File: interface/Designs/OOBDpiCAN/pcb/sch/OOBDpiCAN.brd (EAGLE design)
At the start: 65.1 x 57.3 mm, 143 parts, among them IC1 ADM3053M, IC5 DS3231, IC6 EEPROM24, IC7 ADM3053M, Q1 12MHz, Q2 16MHz

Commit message: first roughly placing of ADM3053
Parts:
- removed $$U$13, U$11, U$9: MCP2551SO8, can:SO08
- removed BAT2: (no value), SparkFun:BATTCON_12MM_PTH
- removed C61: 10u, rcl:C0805K
- removed C62: 100n, rcl:C0805K
- removed U$10, U$12, U$7: (no value), SparkFun-Connectors:SCREWTERMINAL-3.5MM-3
- removed U$6: STM32F042CT, micro-stm_v3:LQFP48
- removed U$8: (no value), jumper:JP5
- added BAT1: (no value), SparkFun:BATTCON_12MM_PTH
- added C47: NA(47nF), resistor:C0603
- added C48: NA(10nF), resistor:C0603
- added C49: 33pF, resistor:C0603
- added C52: 100nF, resistor:C0603
- added IC10, IC3, IC4, IC9: MCP2551SO8, can:SO08
- added IC11: EEPROM24, FLYFISH:SOIC8
- added IC12: DS3231, DS3231_industrialberry:SOIC-16W
- added IC2, IC8: STM32F042CT, micro-stm_v3:LQFP48
- C1, C2: value 33pF -> 100nF
- C11, C12: value 100nF -> 18pF
- C13, C14, C19, C20: value 100nF -> 100n; device resistor:C0603 -> rcl:C0603K
- C15, C16, C27, C29: value 100nF -> 10u; device resistor:C0603 -> rcl:C0805K
- C17, C18: value 100nF -> 10n; device resistor:C0603 -> rcl:C0603K
- C23, C24: value 100nF -> NA (AY2221K29Y5SS63L7); device resistor:C0603 -> rcl:C075-032X103
- C25, C26: value 100nF -> 100n; device resistor:C0603 -> rcl:C0805K
- C28: value 22uF/6.3V -> NA(10nF); device rcl:SMC_A -> resistor:C0603
- C30: value 18pF -> NA(10nF)
- C31: value 18pF -> 10n; device resistor:C0603 -> rcl:C0805K
- C32: value 100nF -> 10n; device resistor:C0603 -> rcl:C0805K
- C33: value 1uF -> 100n; device resistor:C0603 -> rcl:C0805K
- C34: value 10n -> 100n; device rcl:C0603K -> rcl:C0805K
- C35, C38: value 100n -> 100nF; device rcl:C0603K -> resistor:C0603
- C36, C43, C57: value 10u -> 100nF; device rcl:C0805K -> resistor:C0603
- C37, C41: value NA(10nF) -> 100nF
- C39, C44, C59: value 100n -> 100nF; device rcl:C0805K -> resistor:C0603
- C42: value 10n -> 100nF; device rcl:C0805K -> resistor:C0603
- C46: value NA(47nF) -> 100nF
- C50: device resistor:C0603 -> rcl:C0603
- C51: value NA(10nF) -> 33pF
- C53: value 1uF -> 100nF; device rcl:C0603 -> resistor:C0603
- C54: device rcl:C0603 -> resistor:C0603
- C55: value 10n -> 1uF; device rcl:C0603K -> resistor:C0603
- C56: value 100n -> 1uF; device rcl:C0603K -> rcl:C0603
- C58: value 100n -> 22uF/6.3V; device rcl:C0603K -> rcl:SMC_A
- C60: value 10n -> 22uF/6.3V; device rcl:C0805K -> rcl:SMC_A
- C9: value 22uF/6.3V -> 100nF; device rcl:SMC_A -> resistor:C0603
- IC1, IC7: value ADM3053M -> STM32F042CT; device ADM3053:SO20W -> micro-stm_v3:LQFP48
- IC5: value DS3231 -> ADM3053M; device DS3231_industrialberry:SOIC-16W -> ADM3053:SO20W
- IC6: value EEPROM24 -> ADM3053M; device FLYFISH:SOIC8 -> ADM3053:SO20W
- LED2, LED4: value yellow -> green
- LED5, LED7: value green -> yellow
- Q1: value 12MHz -> 16MHz
- Q2: value 16MHz -> 12MHz
- R1, R2: value 10k -> 510R
- R10: value 510R -> 0R; device resistor:R0603 -> rcl:0207/10
- R11: value 510R -> 8.2k; device resistor:R0603 -> rcl:R0603
- R12: value 120R -> 8.2k; device resistor:R0603 -> rcl:R0603
- R13, R14, R15: value 120R -> 60R
- R16: value 10k -> 60R
- R17: value NA(47k) -> 510R
- R18: value 680R -> 510R
- R19: value 10k -> 120R
- R20, R21, R22: value 60R -> 120R
- R27: value 10k -> 680R; device rcl:R0603 -> resistor:R0603
- R3, R4: value 510R -> 120R
- R31: value 8.2k -> 10k; device rcl:R0603 -> resistor:R0603
- R32: value 8.2k -> NA(47k); device rcl:R0603 -> resistor:R0603
- R33, R34, R36: value 0R -> 10k; device rcl:0207/10 -> resistor:R0603
- R35: value 0R -> 10k; device rcl:0207/10 -> rcl:R0603
- R7, R8: value 120R -> 0R; device resistor:R0603 -> rcl:0207/10
- R9: value 60R -> 0R; device resistor:R0603 -> rcl:0207/10
- U$1: value MCP2551SO8 -> (none); device can:SO08 -> jumper:JP5
- U$2, U$4: value STM32F042CT -> (none); device micro-stm_v3:LQFP48 -> SparkFun-Connectors:SCREWTERMINAL-3.5MM-3
- U$3: value GL850G-31 -> (none); device pimoroni:TSSOP28 -> SparkFun-Connectors:SCREWTERMINAL-3.5MM-3
- U$5: value STM32F042CT -> GL850G-31; device micro-stm_v3:LQFP48 -> pimoroni:TSSOP28
- moved C23 136.9 mm to (41.3, 17.8), turned to 90 degrees
- moved C41 125.9 mm to (-105.4, 45.7)
- moved C24 125.1 mm to (22.9, 17.8), turned to 90 degrees
- moved C57 121.8 mm to (-95.2, 39.4), turned to 0 degrees
- moved C54 119.9 mm to (-88.9, 39.4)
- moved R36 117.7 mm to (-88.9, 33.0), turned to 0 degrees
- moved C37 115.3 mm to (-80.0, 45.7)
- moved R16 112.3 mm to (25.4, 6.99)
- moved JP7 110.9 mm to (57.1, 7.62), turned to 90 degrees
- moved JP8 110.9 mm to (50.8, 7.62), turned to 90 degrees
- moved R23 100.5 mm to (-8.89, 39.4)
- moved R24 100.5 mm to (-109.2, 33.0)
- moved C38 98.4 mm to (-86.4, 45.7)
- moved C28 97.3 mm to (14.6, 7.62)
- moved R15 95.6 mm to (25.4, 9.53)
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- renumbered $$U$14 to $$U$1, SJ2 to SJ1
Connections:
- net +3V3: now also C1.1, C18.1, C2.1, C3.1, C36.1, C37.1, C38.1, C39.1, C4.1, C40.1, C41.1, C42.1, C43.1, C44.1, C5.1, C56.2, C6.1, C9.1, IC1.1, IC1.24, IC1.36, IC1.48, IC1.9, IC12.2, IC2.1, IC2.24, IC2.36, IC2.48, IC2.9, IC5.6, IC6.6, IC7.1, IC7.24, IC7.36, IC7.48, IC7.9, IC8.1, IC8.24, IC8.36, IC8.48, IC8.9, JP6.1, R35.2, U$1.1; no longer C11.1, C12.1, C13.1, C14.1, C15.1, C16.1, C21.1, C22.1, C23.1, C24.1, C25.1, C26.1, C27.1, C29.1, C34.1, C53.2, C55.1, C56.1, IC1.6, IC5.2, IC7.6, JP4.1, R27.2, U$2.1, U$2.24, U$2.36, U$2.48, U$2.9, U$4.1, U$4.24, U$4.36, U$4.48, U$4.9, U$5.1, U$5.24, U$5.36, U$5.48, U$5.9, U$6.1, U$6.24, U$6.36, U$6.48, U$6.9, U$8.1
- net +5V: now also C13.1, C14.1, C15.1, C16.1, C21.1, C22.1, C46.1, C50.2, C59.1, C60.+, IC10.3, IC11.8, IC3.3, IC4.3, IC5.8, IC9.3, R31.1, U$5.23; no longer $$U$13.3, C18.1, C28.+, C32.1, C36.1, C38.1, C40.1, C50.1, C54.2, C57.1, C58.1, IC1.8, IC7.8, R16.1, U$1.3, U$11.3, U$3.23, U$9.3
- net BOOT0: now also IC1.44, IC2.44, IC7.44, IC8.44, JP6.2, R1.2, R17.2, R18.2, R2.2; no longer JP4.2, R10.2, R11.2, R3.2, R4.2, U$2.44, U$4.44, U$5.44, U$6.44
- net CAN0-H: now also IC5.17, R14.1, R8.2, U$2.2; no longer IC7.17, R21.1, R34.2, U$10.2
- net CAN0-L: now also IC5.15, JP3.2, R7.2, U$2.1; no longer IC7.15, JP6.2, R33.2, U$10.1
- net CAN0_RXD: now also IC1.45, IC3.4, IC5.4; no longer IC7.4, U$2.45, U$9.4
- net CAN0_TXD: now also IC1.46, IC3.1, IC5.5; no longer IC7.5, U$2.46, U$9.1
- net CAN1-H: now also IC6.17, R10.2, R16.1, U$3.2; no longer IC1.17, R20.1, R36.2, U$7.2
- net CAN1-L: now also IC6.15, JP4.2, R9.2, U$3.1; no longer IC1.15, JP3.2, R35.2, U$7.1
- net CAN1_RXD: now also IC2.45, IC4.4, IC6.4; no longer IC1.4, U$1.4, U$4.45
- net CAN1_TXD: now also IC2.46, IC4.1, IC6.5; no longer IC1.5, U$1.1, U$4.46
- net CAN2-H: now also IC9.7, R24.1, U$4.2; no longer R23.1, U$11.7, U$12.2
- net CAN2-L: now also IC9.6, U$4.1; no longer U$11.6, U$12.1
- net CAN3-H: now also IC10.7, R26.1; no longer $$U$13.7, R25.1
- net CAN3-L: now also IC10.6; no longer $$U$13.6
- net GND: now also BAT1.GND, C23.1, C24.1, C28.2, C39.2, C42.2, C43.2, C44.2, C47.2, C48.2, C49.2, C50.1, C52.2, C53.2, C54.2, C56.1, C58.-, C59.2, C60.-, C9.2, IC1.23, IC1.35, IC1.47, IC1.8, IC10.2, IC10.8, IC11.1, IC11.2, IC11.3, IC11.4, IC12.10, IC12.11, IC12.12, IC12.13, IC12.5, IC12.6, IC12.7, IC12.8, IC12.9, IC2.23, IC2.35, IC2.47, IC2.8, IC3.2, IC3.8, IC4.2, IC4.8, IC5.1, IC5.3, IC6.10, IC6.7, IC6.9, IC7.23, IC7.35, IC7.47, IC7.8, IC8.23, IC8.35, IC8.47, IC8.8, IC9.2, IC9.8, R1.1, R2.1, R20.1, R21.1, R22.1, R27.1, R32.1, R36.1, U$1.3, U$2.3, U$3.3, U$4.3, U$5.14, U$5.15; no longer $$U$13.2, $$U$13.8, BAT2.GND, C23.2, C24.2, C25.2, C26.2, C27.2, C28.-, C29.2, C31.2, C32.2, C33.2, C34.2, C50.2, C53.1, C54.1, C56.2, C58.2, C9.-, IC1.1, IC1.10, IC1.3, IC1.7, IC1.9, IC5.11, IC5.12, IC5.13, IC5.5, IC5.6, IC5.8, IC6.2, IC6.4, IC7.1, IC7.10, IC7.3, IC7.7, IC7.9, R10.1, R11.1, R12.1, R13.1, R14.1, R15.1, R7.1, R8.1, U$1.2, U$1.8, U$10.3, U$11.2, U$11.8, U$12.3, U$2.23, U$2.35, U$2.47, U$2.8, U$3.14, U$3.15, U$4.23, U$4.35, U$4.47, U$4.8, U$5.23, U$5.35, U$5.47, U$5.8, U$6.23, U$6.35, U$6.47, U$6.8, U$7.3, U$8.3, U$9.2, U$9.8
- net GNDA: now also C23.2, C24.2, C25.2, C26.2, C27.2, C29.2, C31.2, C32.2, C33.2, C34.2, IC5.11, IC5.13, IC5.16, IC5.20, IC6.11, IC6.13, IC6.16, IC6.20, R11.1, R12.1; no longer C39.2, C42.2, C43.2, C44.2, C59.2, C60.2, C61.2, C62.2, IC1.11, IC1.13, IC1.16, IC1.20, IC7.11, IC7.13, IC7.16, IC7.20, R31.1, R32.1
- net ID_SC: now also IC11.6, R29.2; no longer IC6.6, R28.2
- net ID_SD: now also IC11.5, R30.2; no longer IC6.5, R29.2
- net INT-: now also IC12.3, R35.1; no longer IC5.3, R27.1
- net MC0_1: now also IC2.29, IC7.5; no longer U$4.29, U$5.5
- net MCO_0: now also IC1.29; no longer U$2.29
- net MCO_1: now also IC2.5; no longer U$4.5
- net MCO_2: now also IC7.29, IC8.5; no longer U$5.29, U$6.5
- net N$1: now also IC5.18, R11.2; no longer IC7.18, R31.2
- net N$10: now also C12.1, IC1.6, Q1.2; no longer C31.1, Q2.2, U$2.6
- net N$11: now also C11.1, IC1.5, Q1.1; no longer C30.1, Q2.1, U$2.5
- net N$12: now also IC6.18, R12.2; no longer IC1.18, R32.2
- net N$13: now also C26.1, C29.1, C32.1, C34.1, IC6.12, IC6.19; no longer C39.1, C42.1, C43.1, C44.1, IC1.12, IC1.19
- net N$14: now also IC3.6, R7.1; no longer R33.1, U$9.6
- net N$15: now also IC8.19, LED7.A; no longer LED4.A, U$6.19
- net N$16: now also IC8.18; no longer U$6.18
- net N$17: now also LED7.C, R21.2; no longer LED4.C, R14.2
- net N$18: now also R22.2; no longer R15.2
- net N$19: now also IC3.7, R8.1; no longer R34.1, U$9.7
- net N$2: now also C51.1, Q2.2, U$5.7; no longer C1.1, Q1.2, U$3.7
- net N$20: now also C47.1; no longer C46.1
- net N$21: now also IC10.4, IC8.45; no longer $$U$13.4, U$6.45
- net N$22: now also IC1.19; no longer U$2.19
- net N$23: now also IC1.18, LED2.A; no longer LED5.A, U$2.18
- net N$24: now also R3.2; no longer R5.2
- net N$25: now also LED2.C, R4.2; no longer LED5.C, R6.2
- net N$26: now also IC4.7, R10.1; no longer R36.1, U$1.7
- net N$27: now also IC4.6, R9.1; no longer R35.1, U$1.6
- net N$28: now also JP4.1, R15.1; no longer JP3.1, R9.1
- net N$29: now also IC2.19, LED3.A; no longer LED2.A, U$4.19
- net N$3: now also C49.1, Q2.1, U$5.6; no longer C2.1, Q1.1, U$3.6
- net N$30: now also IC2.18, LED4.A; no longer LED6.A, U$4.18
- net N$31: now also LED3.C, R5.2; no longer LED2.C, R7.2
- net N$32: now also LED4.C, R6.2; no longer LED6.C, R8.2
- net N$33: now also C57.1, C58.+, R33.2, R34.2, U$5.16, U$5.24; no longer C6.1, C9.+, R1.2, R2.2, U$3.16, U$3.24
- net N$34: now also R33.1, U$5.18; no longer R2.1, U$3.18
- net N$35: now also R34.1, U$5.17; no longer R1.1, U$3.17
- net N$36: now also C55.1, R31.2, R32.2, U$5.13; no longer C33.1, R16.2, R17.2, U$3.13
- net N$37: now also U$5.26; no longer U$3.26
- net N$38: now also U$5.25; no longer U$3.25
- net N$39: now also C52.1, C53.1, C54.1, U$5.1, U$5.10, U$5.5; no longer C3.1, C4.1, C5.1, U$3.1, U$3.10, U$3.5
- net N$4: now also IC7.19, LED5.A; no longer LED3.A, U$5.19
- net N$40: now also R27.2, U$5.4; no longer R18.2, U$3.4
- net N$44: now also R36.2; no longer R19.2
- net N$48: now also JP3.1, R13.1; no longer JP6.1, R22.1
- net N$49: now also C30.1, R15.2, R16.2; no longer C37.1, R20.2, R9.2
- net N$5: now also IC11.7, R28.2; no longer IC6.7, R30.2
- net N$53: now also C28.1, R13.2, R14.2; no longer C41.1, R21.2, R22.2
- net N$54: now also IC10.1, IC8.46; no longer $$U$13.1, U$6.46
- net N$56: now also IC7.45, IC9.4; no longer U$11.4, U$5.45
- net N$57: now also IC7.46, IC9.1; no longer U$11.1, U$5.46
- net N$59: now also R25.1; no longer R26.1
- net N$6: now also R23.1; no longer R24.1
- net N$63: now also C48.1; no longer C51.1
- net N$65: now also C25.1, C27.1, C31.1, C33.1, IC5.12, IC5.19; no longer C59.1, C60.1, C61.1, C62.1, IC7.12, IC7.19
- net N$7: now also IC7.18, LED6.A; no longer LED7.A, U$5.18
- net N$8: now also LED5.C, R19.2; no longer LED3.C, R12.2
- net N$9: now also LED6.C, R20.2; no longer LED7.C, R13.2
- net NRST: now also IC1.7, IC2.7, IC7.7, U$1.5; no longer U$2.7, U$4.7, U$5.7, U$8.5
- net NRST1: now also IC8.7; no longer U$6.7
- net SCL: now also IC12.16; no longer IC5.16
- net SDA: now also IC12.15; no longer IC5.15
- net SWCLK: now also IC1.37, IC2.37, IC7.37, U$1.2; no longer U$2.37, U$4.37, U$5.37, U$8.2
- net SWCLK1: now also IC8.37; no longer U$6.37
- net SWDIO: now also IC1.34, IC2.34, IC7.34, U$1.4; no longer U$2.34, U$4.34, U$5.34, U$8.4
- net SWDIO1: now also IC8.34; no longer U$6.34
- net USB0_DM: now also IC1.32, U$5.27; no longer U$2.32, U$3.27
- net USB0_DP: now also IC1.33, U$5.28; no longer U$2.33, U$3.28
- net USB1_DM: now also IC2.32, U$5.2; no longer U$3.2, U$4.32
- net USB1_DP: now also IC2.33, U$5.3; no longer U$3.3, U$4.33
- net USB2_DM: now also IC7.32, U$5.8; no longer U$3.8, U$5.32
- net USB2_DP: now also IC7.33, U$5.9; no longer U$3.9, U$5.33
- net USB3_DM: now also IC8.32, U$5.11; no longer U$3.11, U$6.32
- net USB3_DP: now also IC8.33, U$5.12; no longer U$3.12, U$6.33
- net VBAT: now also BAT1.VCC@1, IC12.14; no longer BAT2.VCC@1, IC5.14

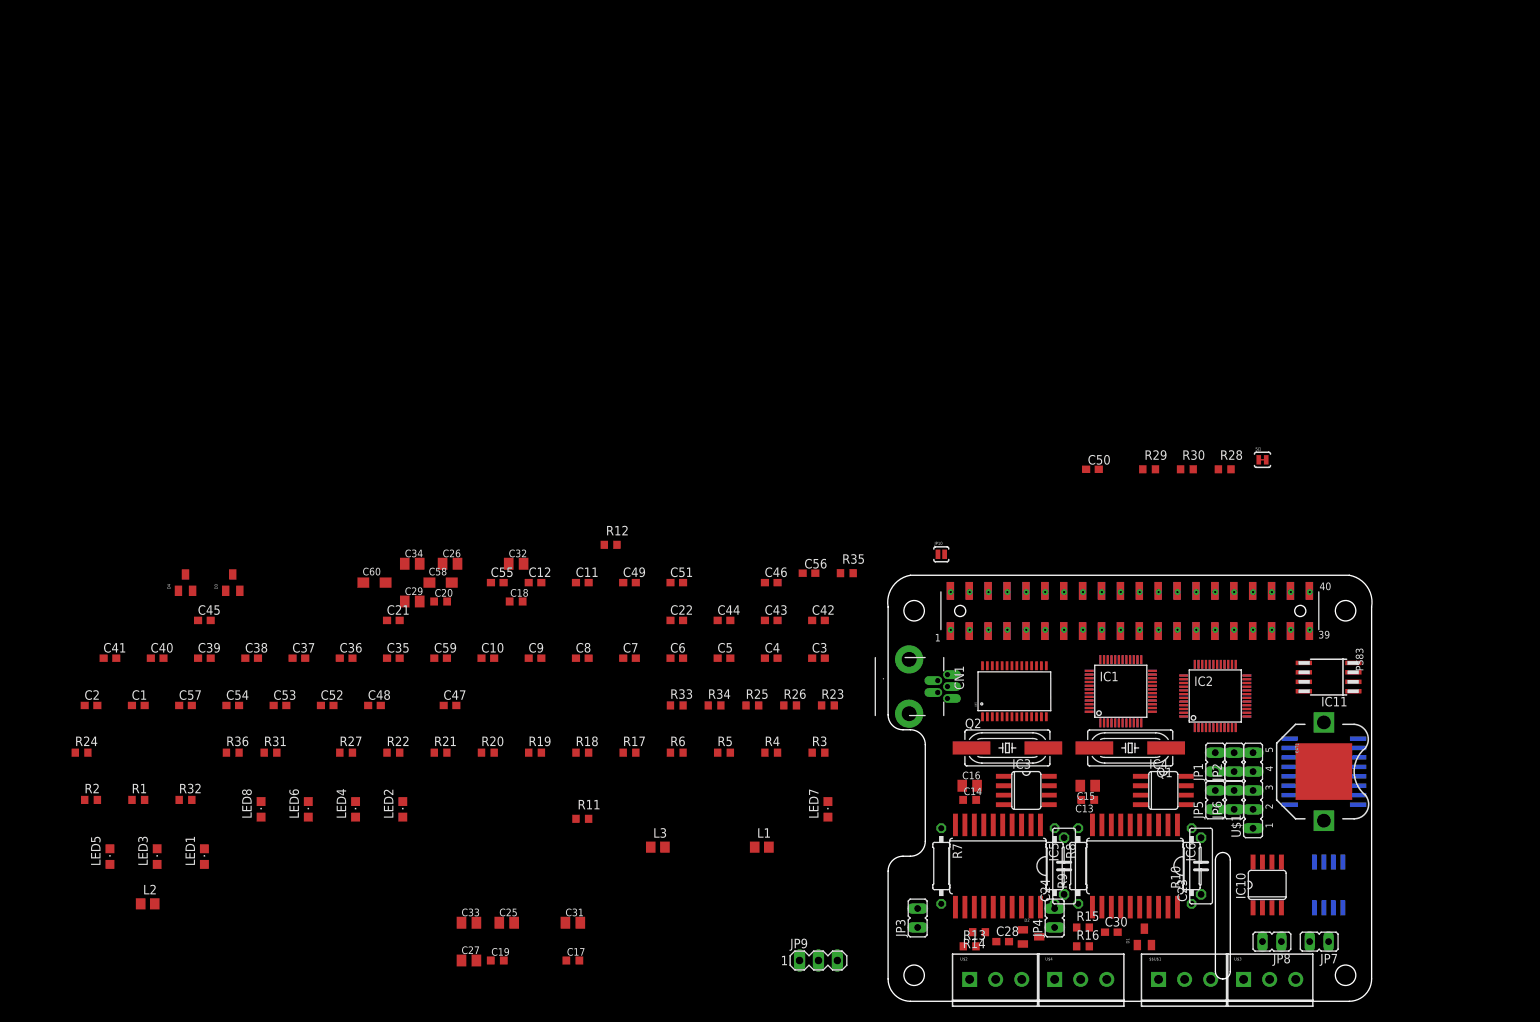
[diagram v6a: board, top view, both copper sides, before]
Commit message: - create initial PDF of latest schematics - start placing and routing of CAN-Interfaces
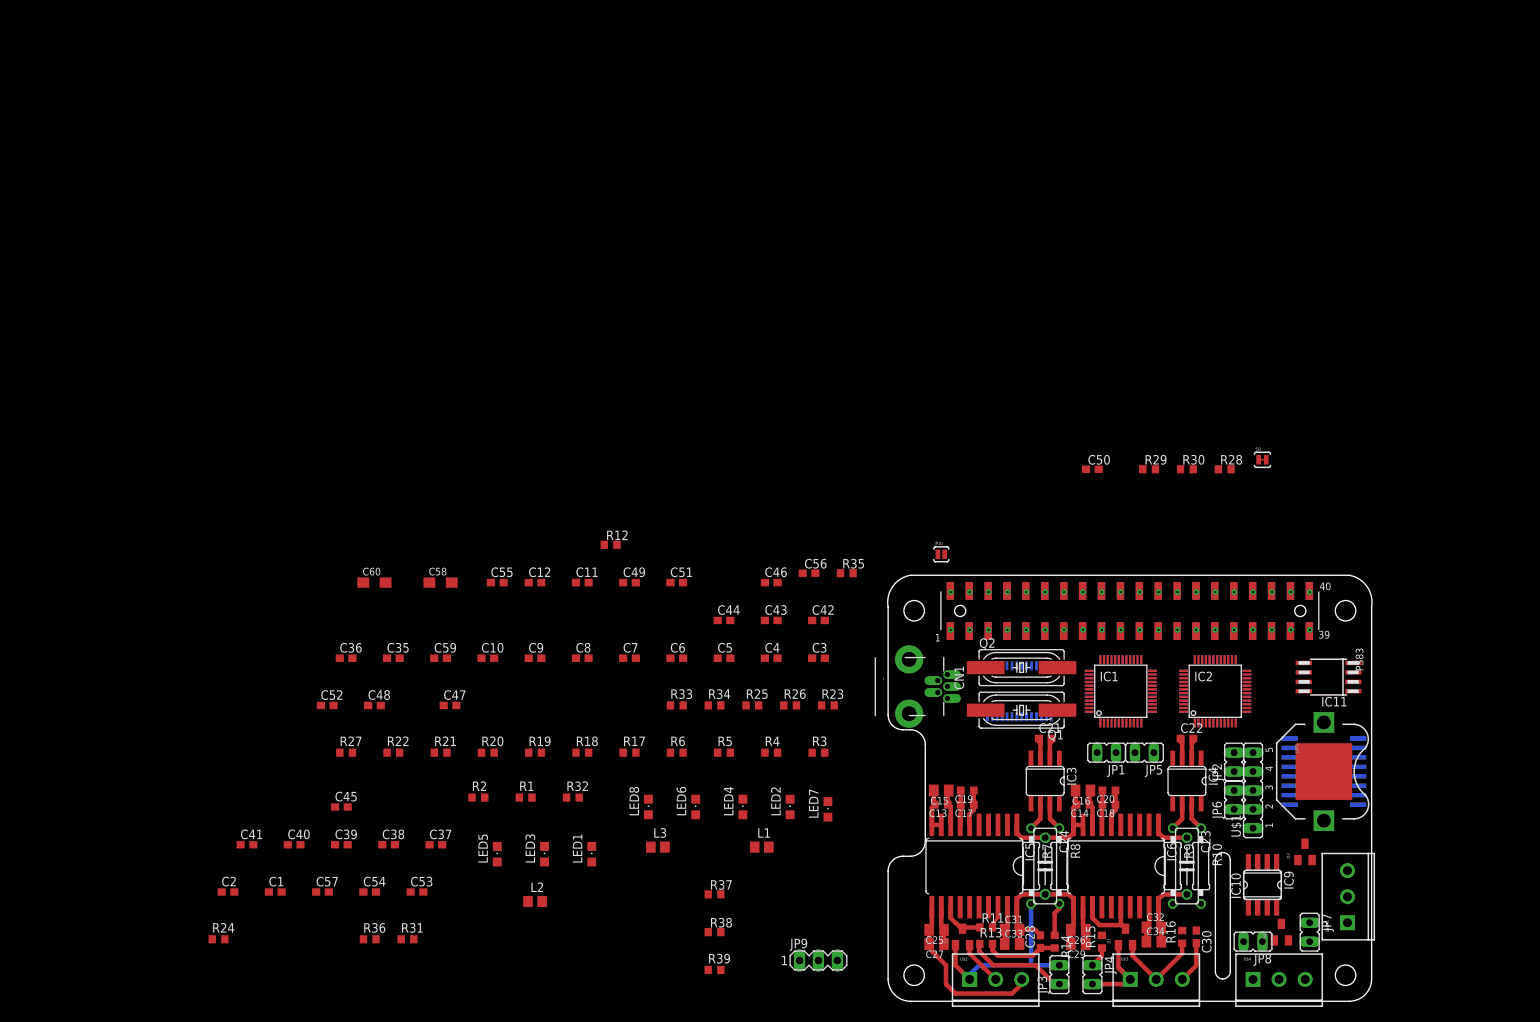
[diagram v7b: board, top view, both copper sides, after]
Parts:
- added R37, R38: 0R, rcl:R0603
- added R39: 0R, resistor:R0603
- moved D4 154.6 mm to (52.1, 8.89)
- moved D3 148.6 mm to (55.2, 19.7)
- moved C34 111.9 mm to (34.9, 7.62)
- moved C29 100.7 mm to (24.8, 7.30), turned to 180 degrees
- moved C32 98.7 mm to (34.9, 9.53)
- moved C26 97.7 mm to (24.8, 9.21), turned to 180 degrees
- moved C20 93.4 mm to (28.9, 27.9), turned to 180 degrees
- moved C21 89.1 mm to (20.3, 34.9)
- moved C18 84.2 mm to (28.9, 26.0), turned to 180 degrees
- moved C33 73.1 mm to (15.9, 7.30)
- moved C22 70.4 mm to (39.4, 34.9)
- moved C19 67.2 mm to (9.84, 27.9), turned to 180 degrees
- moved C27 62.9 mm to (5.71, 7.30), turned to 180 degrees
- moved C31 59.1 mm to (15.9, 9.21)
- moved C25 57.8 mm to (5.71, 9.21), turned to 180 degrees
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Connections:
- new net N$43: IC1.29, R37.2
- new net N$45: IC2.29, R38.2
- new net N$46: IC7.29, R39.1
- net GND: no longer C28.2, C30.2, D1.3, D2.3, U$2.3, U$3.3
- net GNDA: now also C28.2, C30.2, D1.3, D2.3, U$2.3, U$3.3
- net MC0_1: now also R38.1; no longer IC2.29
- net MCO_0: now also R37.1; no longer IC1.29
- net MCO_2: now also R39.2; no longer IC7.29
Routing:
- net GNDA: track 0.00 -> 76.8 mm
- net GND: track 0.00 -> 42.5 mm
- net CAN0-L: track 0.00 -> 26.9 mm
- net +5V: track 0.00 -> 15.2 mm
- net N$48: track 0.00 -> 13.6 mm
- net CAN1-L: track 0.00 -> 12.9 mm
- net CAN1-H: track 0.00 -> 12.2 mm
- net CAN0-H: track 0.00 -> 10.6 mm
- net N$65: track 0.00 -> 10.2 mm
- net N$53: track 0.00 -> 9.95 mm
- net +3V3: track 0.00 -> 9.72 mm
- net N$13: track 0.00 -> 9.21 mm
- net N$19: track 0.00 -> 3.80 mm
- net N$14: track 0.00 -> 3.80 mm
- net N$27: track 0.00 -> 3.80 mm
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
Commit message: add latest modifications to OOBD schematics
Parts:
- R11, R12: value 8.2k -> 8k2
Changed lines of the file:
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@@
 <element name="C15" library="rcl" package="C0805K" value="10u" x="6.35" y="27.94" rot="R180"/>
 <element name="C13" library="rcl" package="C0603K" value="100n" x="6.35" y="26.035" rot="R180"/>
-<element name="R11" library="rcl" package="R0603" value="8.2k" x="12.3825" y="9.525"/>
+<element name="R11" library="rcl" package="R0603" value="8k2" x="12.3825" y="9.525"/>
 <element name="C33" library="rcl" package="C0805K" value="100n" x="15.875" y="7.3025"/>
 <element name="C31" library="rcl" package="C0805K" value="10n" x="15.875" y="9.2075"/>
@@
 <element name="C16" library="rcl" package="C0805K" value="10u" x="25.4" y="27.94" rot="R180"/>
 <element name="C14" library="rcl" package="C0603K" value="100n" x="25.4" y="26.035" rot="R180"/>
-<element name="R12" library="rcl" package="R0603" value="8.2k" x="-38.1" y="60.96"/>
+<element name="R12" library="rcl" package="R0603" value="8k2" x="-38.1" y="60.96"/>
 <element name="C34" library="rcl" package="C0805K" value="100n" x="34.925" y="7.62"/>
 <element name="C32" library="rcl" package="C0805K" value="10n" x="34.925" y="9.525"/>
